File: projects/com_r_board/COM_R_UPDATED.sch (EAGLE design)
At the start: 18 parts, among them J1 0532610471, J2 53398-1271, J3 504050-0691, J4 ESQ-126-39-G-D, J5 ESQ-126-39-G-D, J6 G125-MS10605L3P

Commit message: COM_R revision 1. 12/8/2020
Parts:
- removed R1, R2, R4: 1k, rcl:R-US_M0805
- removed U$2: DF13-4P-1.25V, con-hirose-df13:DF13-4P-1.25V
- added J7: 61300411121, SamacSys_Parts:61300411121
- added R3: TNPW080510K0BETY, TNPW080510K0BETY:TNPW080510K0BETY
- added R6, R7: Y40621K00000Q0R, Y40621K00000Q0R:Y40621K00000Q0R
- PWR_LED, RX_LED, TX_LED: value (none) -> HSMQ-C170-T0000; device led:LEDCHIP-LED0805 -> SamacSys_Parts:HSMQ-C170-T0000
- R5: value 10k -> Y40621K00000Q0R; device rcl:R-US_WSC01/2 -> Y40621K00000Q0R:Y40621K00000Q0R
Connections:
- net PH_NEG renamed PH5_NEG
- net PH_POS renamed PH5_POS
- net PWMA renamed NEG_LEAD
- net PWMB renamed POS_LEAD
- net VCC/5V renamed 5V_BUS
- removed net N$7: PWR_LED.A, R4.1
- removed net VCC/3V3: C2.+, J2.11, J5.17, U$2.1, U$3.P$18, U$3.P$23, U$3.P$24, U$3.P$25, U$3.P$26, U$3.P$27, U$3.P$28
- new net 3V3_COM: C2.+, J2.11, J5.17, J7.2, U$3.P$18, U$3.P$23, U$3.P$24, U$3.P$25, U$3.P$26, U$3.P$27, U$3.P$28
- new net N$2: PWR_LED.A, R7.1
- net GND: now also J7.1, PWR_LED.K, R3.1, RX_LED.K, TX_LED.K; no longer PWR_LED.C, R5.1, RX_LED.C, TX_LED.C, U$2.2
- net N$1: now also R5.1; no longer R1.1
- net N$4: now also R6.1; no longer R2.1
- net PWR_LED: now also R7.2; no longer R4.2
- net RX_LED: now also R6.2; no longer R2.2
- net TX_LED: now also R5.2; no longer R1.2
- net UART_RX: now also J7.4; no longer U$2.4
- net UART_TX: now also J7.3, R3.2; no longer R5.2, U$2.3
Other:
- moved on the sheet: PWR_LED, R5, RX_LED

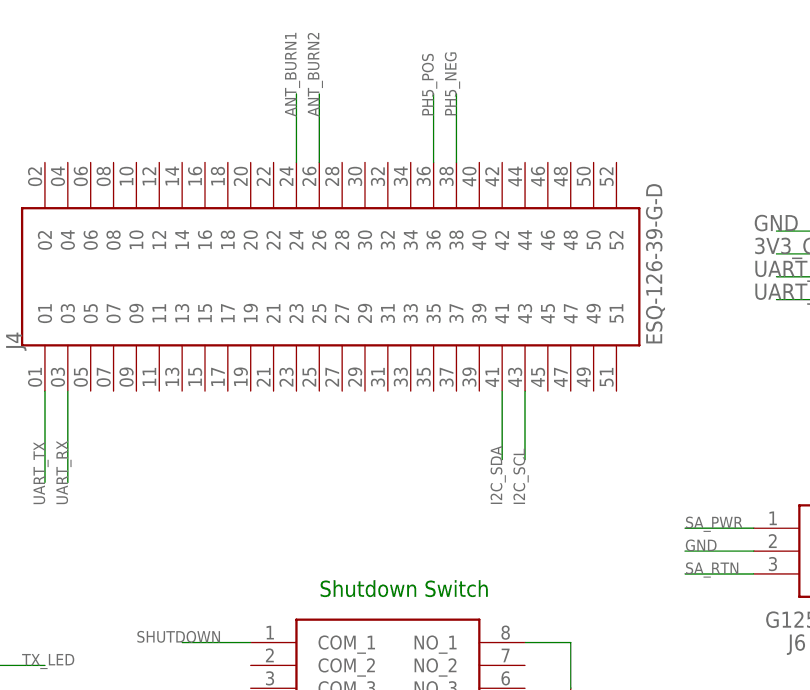
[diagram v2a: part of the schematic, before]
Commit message: Fixed PC104 mounting holes and updated pc104 pinouts to be updated
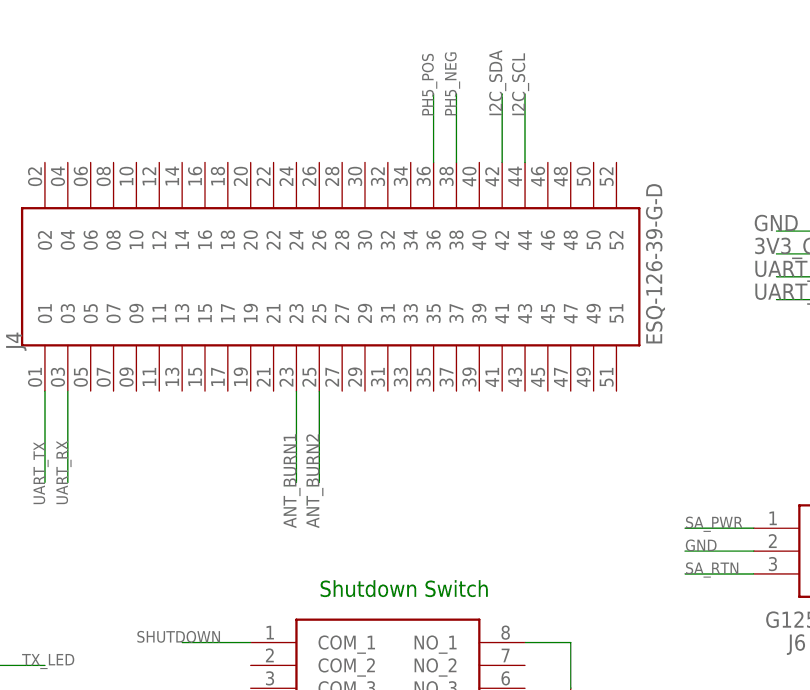
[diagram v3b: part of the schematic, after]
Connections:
- net ANT_BURN1: now also J4.23; no longer J4.24
- net ANT_BURN2: now also J4.25; no longer J4.26
- net I2C_SCL: now also J4.44; no longer J4.43
- net I2C_SDA: now also J4.42; no longer J4.41
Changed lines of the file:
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@@
 <net name="ANT_BURN1" class="0">
-<segment>
-<pinref part="J4" gate="G$1" pin="24"/>
-<wire x1="12.7" y1="68.58" x2="12.7" y2="76.2" width="0.1524" layer="91"/>
-<label x="12.7" y="73.66" size="1.27" layer="95" rot="R90"/>
-</segment>
 <segment>
 <pinref part="J3" gate="G$1" pin="1"/>
@@
 <label x="96.52" y="66.04" size="1.27" layer="95"/>
 </segment>
+<segment>
+<pinref part="J4" gate="G$1" pin="23"/>
+<wire x1="12.7" y1="43.18" x2="12.7" y2="33.02" width="0.1524" layer="91"/>
+<label x="12.7" y="27.94" size="1.4224" layer="95" rot="R90"/>
+</segment>
 </net>
 <net name="ANT_BURN2" class="0">
-<segment>
-<pinref part="J4" gate="G$1" pin="26"/>
-<wire x1="15.24" y1="68.58" x2="15.24" y2="76.2" width="0.1524" layer="91"/>
-<label x="15.24" y="73.66" size="1.27" layer="95" rot="R90"/>
-</segment>
 <segment>
 <pinref part="J3" gate="G$1" pin="2"/>
 <wire x1="104.14" y1="63.5" x2="99.06" y2="63.5" width="0.1524" layer="91"/>
 <label x="96.52" y="63.5" size="1.27" layer="95"/>
+</segment>
+<segment>
+<pinref part="J4" gate="G$1" pin="25"/>
+<wire x1="15.24" y1="43.18" x2="15.24" y2="33.02" width="0.1524" layer="91"/>
+<label x="15.24" y="27.94" size="1.4224" layer="95" rot="R90"/>
 </segment>
 </net>
@@
 </segment>
 <segment>
-<pinref part="J4" gate="G$1" pin="41"/>
-<wire x1="35.56" y1="43.18" x2="35.56" y2="35.56" width="0.1524" layer="91"/>
-<label x="35.56" y="30.48" size="1.27" layer="95" rot="R90"/>
+<pinref part="J4" gate="G$1" pin="42"/>
+<wire x1="35.56" y1="68.58" x2="35.56" y2="76.2" width="0.1524" layer="91"/>
+<label x="35.56" y="73.66" size="1.4224" layer="95" rot="R90"/>
 </segment>
 </net>
@@
 </segment>
 <segment>
-<pinref part="J4" gate="G$1" pin="43"/>
-<wire x1="38.1" y1="43.18" x2="38.1" y2="35.56" width="0.1524" layer="91"/>
-<label x="38.1" y="30.48" size="1.27" layer="95" rot="R90"/>
+<pinref part="J4" gate="G$1" pin="44"/>
+<wire x1="38.1" y1="68.58" x2="38.1" y2="76.2" width="0.1524" layer="91"/>
+<label x="38.1" y="73.66" size="1.4224" layer="95" rot="R90"/>
 </segment>
 </net>
